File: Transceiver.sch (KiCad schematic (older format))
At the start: 37 parts

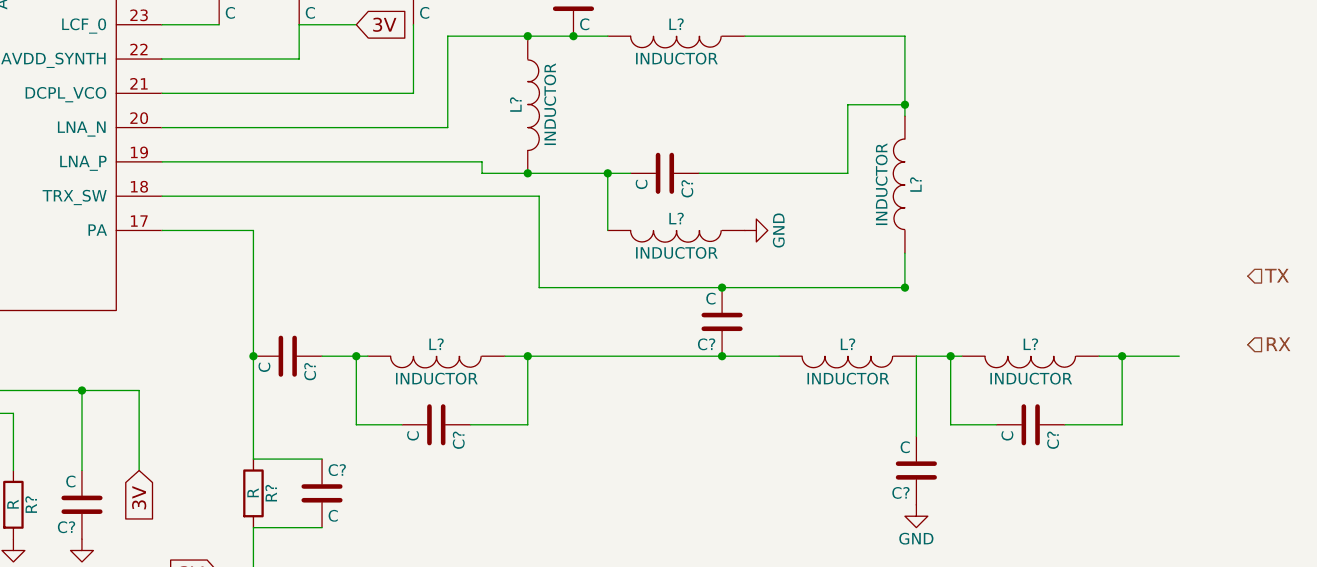
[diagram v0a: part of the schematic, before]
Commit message: took out the mcu schematic, fixed transciever for separate tx rx ports
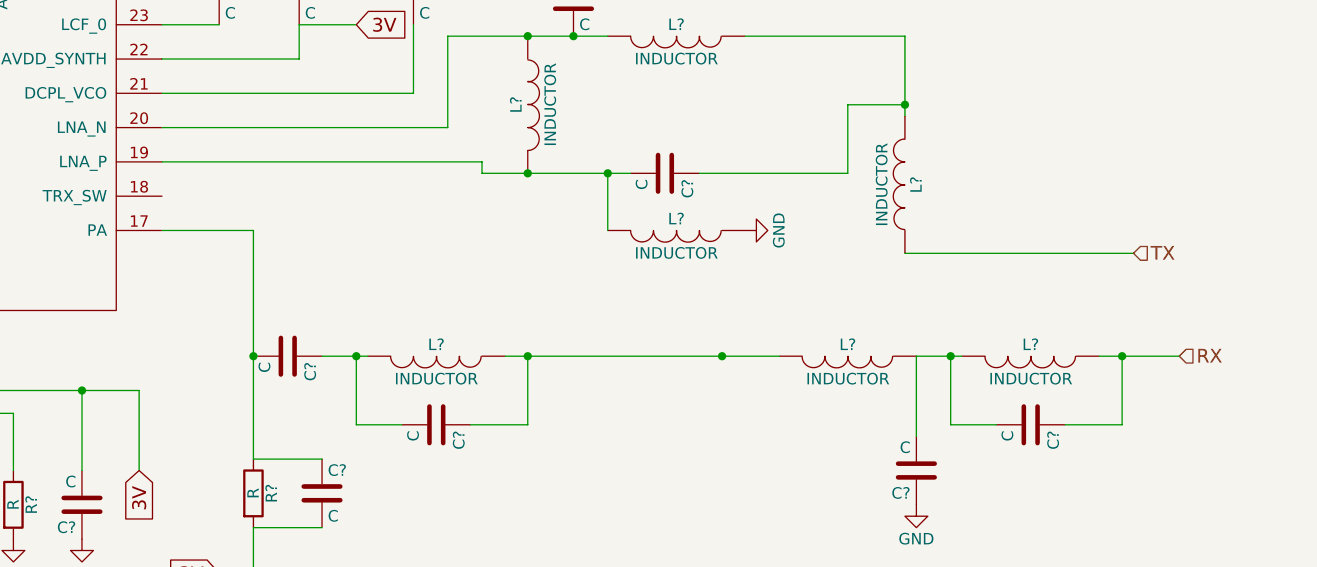
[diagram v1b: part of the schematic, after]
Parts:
- removed C?: C, symbol C
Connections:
- net RX: now also C?.1, L?.1
- net TX: now also L?.1
- net at U?.18 (TRX_SW): no longer L?.1
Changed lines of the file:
@@
-$Comp
-L C C?
-U 1 1 5821C907
-P 7800 4600
-F 0 "C?" H 7825 4700 50  0000 L CNN
-F 1 "C" H 7825 4500 50  0000 L CNN
-F 2 "" H 7838 4450 50  0000 C CNN
-F 3 "" H 7800 4600 50  0000 C CNN
-	1    7800 4600
-	-1   0    0    1
-$EndComp
 $Comp
 L C C?
@@
 Connection ~ 8600 3650
 Wire Wire Line
-	5350 4050 7000 4050
-Wire Wire Line
-	7000 4050 7000 4450
-Wire Wire Line
-	8600 4450 8600 4300
-Connection ~ 8600 4450
-Wire Wire Line
 	5350 4200 5750 4200
 Wire Wire Line
@@
 Wire Wire Line
 	6050 5700 6050 5900
-Wire Wire Line
-	7000 4450 8600 4450
-Connection ~ 7800 4450
 Wire Wire Line
 	4600 4750 4600 4800
@@
 Text HLabel 3850 4750 3    60   Input ~ 0
 CSN
-Text HLabel 10100 4700 2    60   Input ~ 0
+Text HLabel 9800 4750 2    60   Input ~ 0
 RX
-Text HLabel 10100 4400 2    60   Input ~ 0
+Text HLabel 9600 4300 2    60   Input ~ 0
 TX
+Wire Wire Line
+	9600 4300 8600 4300
 $EndSCHEMATC

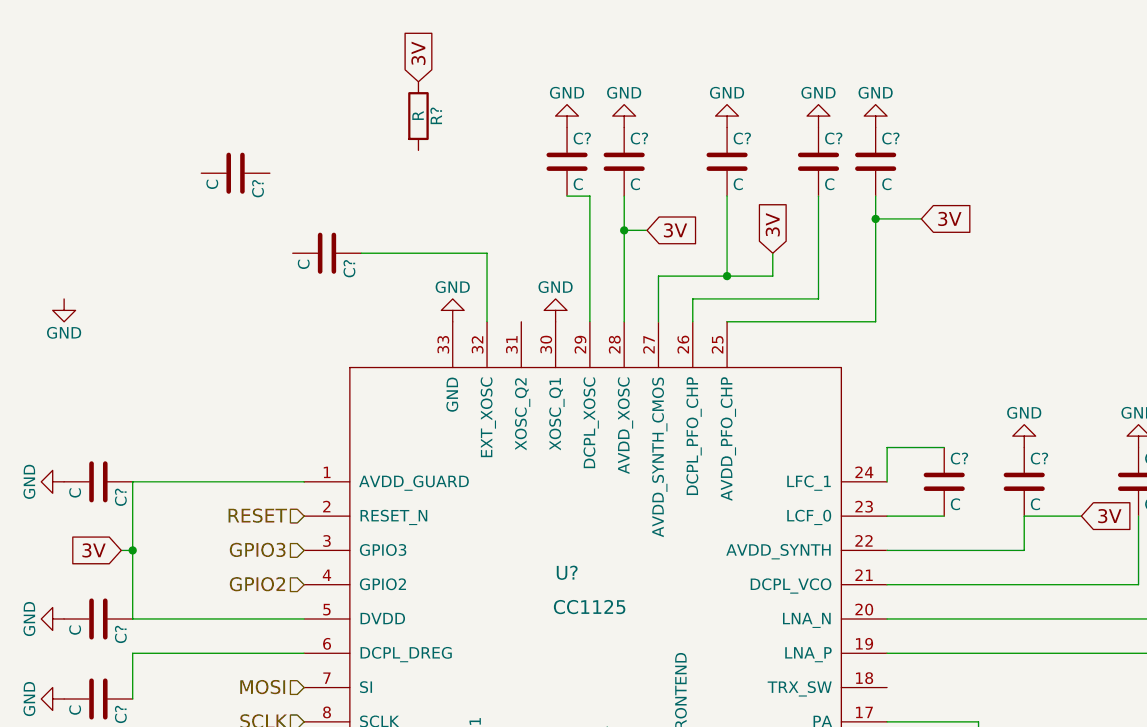
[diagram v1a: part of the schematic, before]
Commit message: deleted MCU schematic for v0.1. Added power sub-schematic
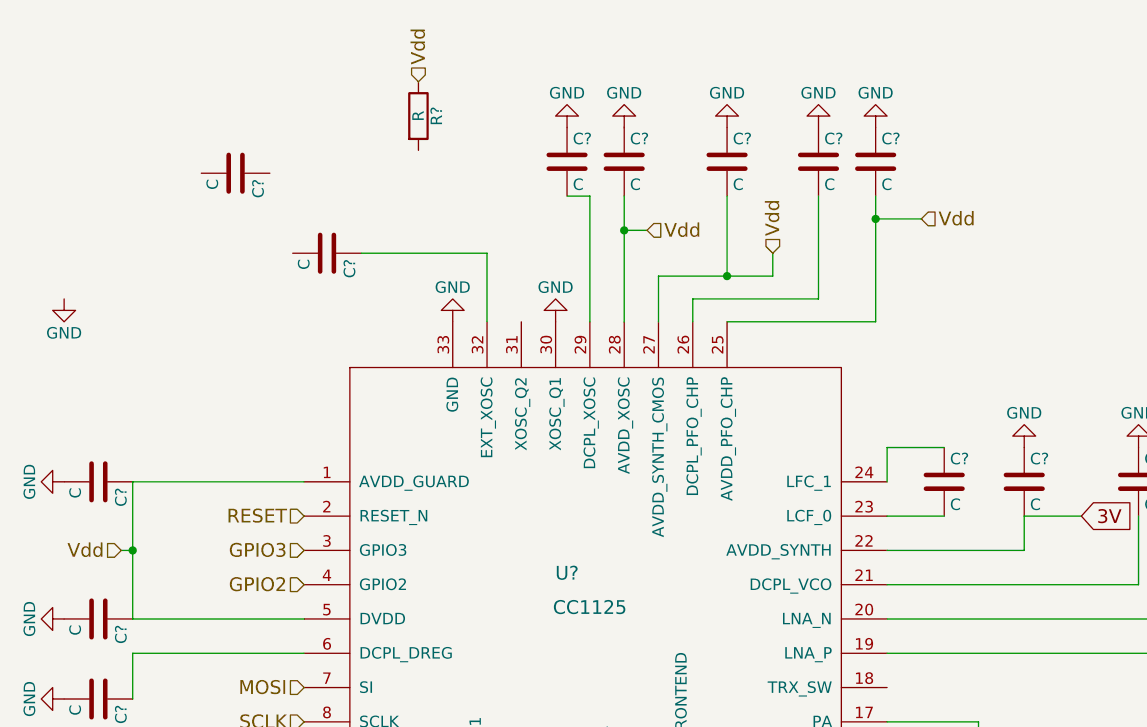
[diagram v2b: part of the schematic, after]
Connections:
- net 3V: no longer C?.1, C?.1, C?.2, C?.2, C?.2, R?.1, U?.1 (AVDD_GUARD), U?.25 (AVDD_PFO_CHP), U?.27 (AVDD_SYNTH_CMOS), U?.28 (AVDD_XOSC), U?.5 (DVDD)
- new net Vdd: C?.1, C?.1, C?.2, C?.2, C?.2, R?.1, U?.1 (AVDD_GUARD), U?.25 (AVDD_PFO_CHP), U?.27 (AVDD_SYNTH_CMOS), U?.28 (AVDD_XOSC), U?.5 (DVDD)
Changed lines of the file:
@@
 	-1   0    0    1
 $EndComp
-Text GLabel 2000 3450 0    60   Input ~ 0
-3V
 $Comp
 L C C?
@@
 	1    0    0    -1
 $EndComp
-Text GLabel 5500 2000 2    60   Input ~ 0
-3V
-Text GLabel 4850 2150 1    60   Input ~ 0
-3V
-Text GLabel 4300 2050 2    60   Input ~ 0
-3V
-Text GLabel 3300 1400 1    60   Input ~ 0
-3V
 Text HLabel 2800 3300 0    60   Input ~ 0
 RESET
@@
 Wire Wire Line
 	9600 4300 8600 4300
+Text HLabel 2000 3450 0    60   Input ~ 0
+Vdd
+Text HLabel 3300 1400 1    60   Input ~ 0
+Vdd
+Text HLabel 4300 2050 2    60   Input ~ 0
+Vdd
+Text HLabel 4850 2150 1    60   Input ~ 0
+Vdd
+Text HLabel 5500 2000 2    60   Input ~ 0
+Vdd
 $EndSCHEMATC

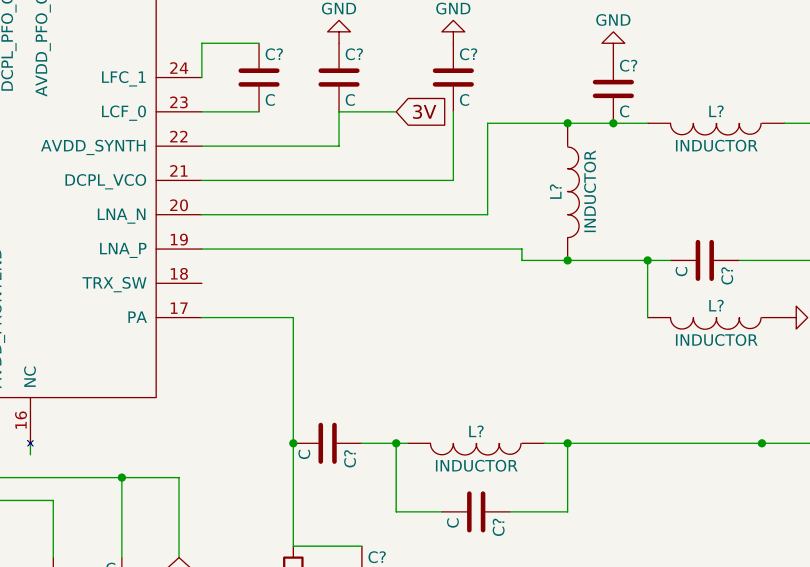
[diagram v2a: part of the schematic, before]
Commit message: added SKY65366-21 schematic and footprint to library. Populated front end schematic with SKY and peripherial components. Added 3V6 output for power sub-schematic.
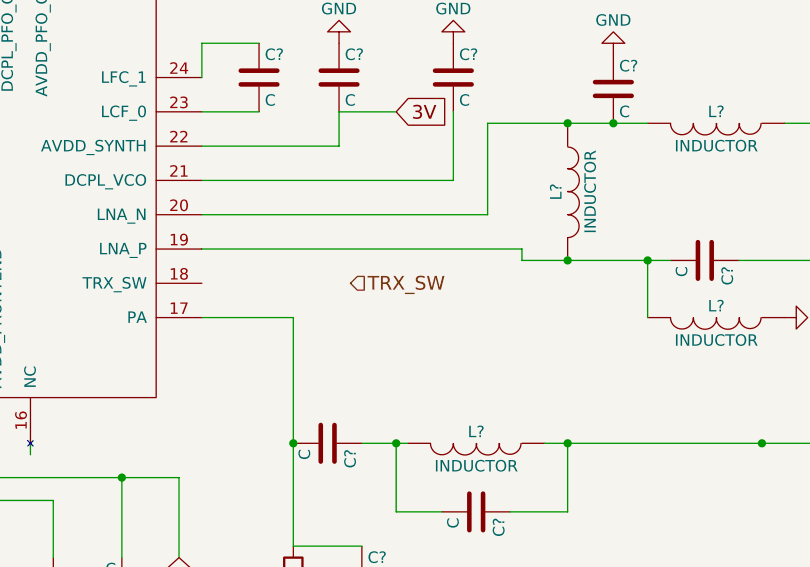
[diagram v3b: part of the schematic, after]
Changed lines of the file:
@@
 Text HLabel 5500 2000 2    60   Input ~ 0
 Vdd
+Text HLabel 6000 4050 2    60   Input ~ 0
+TRX_SW
 $EndSCHEMATC

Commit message: added BALF-112X-02D3 to component library and to transciever sub-schematic
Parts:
- removed C? (x9): C, symbol C
- removed L? (x7): INDUCTOR, symbol INDUCTOR
- removed R?: R, symbol R
- added C? (x2): C, symbol C
- added L?: INDUCTOR, symbol INDUCTOR
- added R?: R, symbol R
- added U?: BALF-112X-02D3, symbol BALF-112X-02D3
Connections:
- net labels added: 3V3, TRX_OPEN, TRX_SIG
- net labels removed: 3V, TRX_SW, Vdd
- wire segments 76 -> 60
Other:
- note added: "Add SPDT RF switch to component \nlibrary and schematic"
- note added: "TRX_OPEN is a active open drain when in TX mode, \nhigh impedence when in RX. TRX_SW requirs active \n3V3 high when in TX mode and GND when in RX \nmode (both low impedence)"
- note added: "add XOSC to component \nlibrary and to schematic\n"
- moved on the sheet: C?, R?, U?

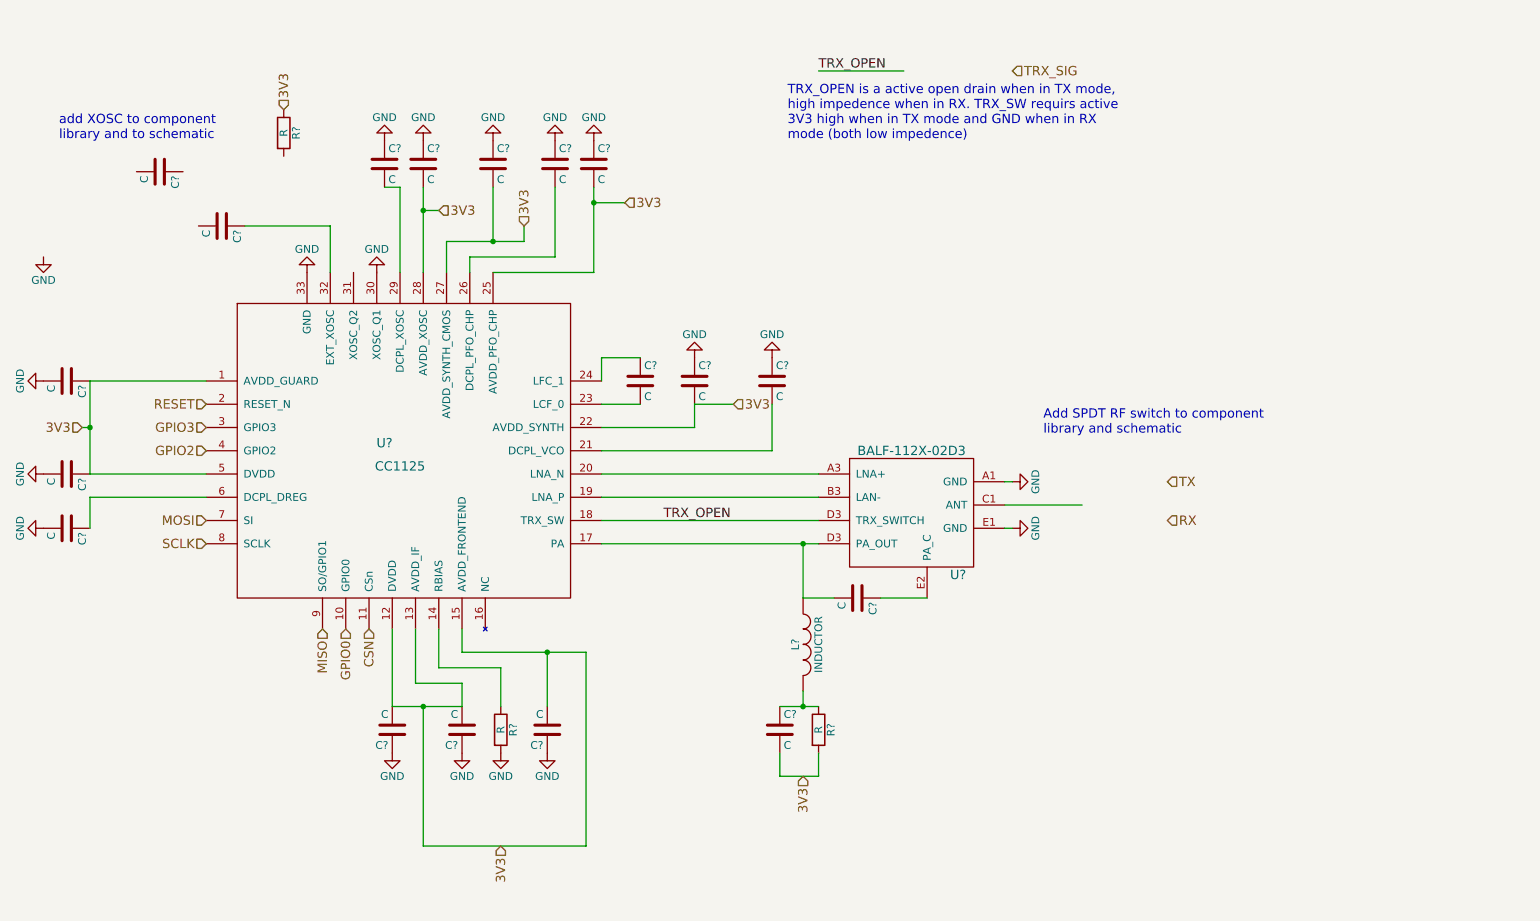
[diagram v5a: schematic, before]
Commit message: Added RF switch to transciever schematic
-Removed SMA lib pointing to Tobi's downloads
-Added SKY13372-467LF to the library (symbol and decal)
-Renamed signal “TX_SW” on RF front end page to “TRX_SIG”
-Re-aligned some part names and reference designators
-Added some component values to the front end
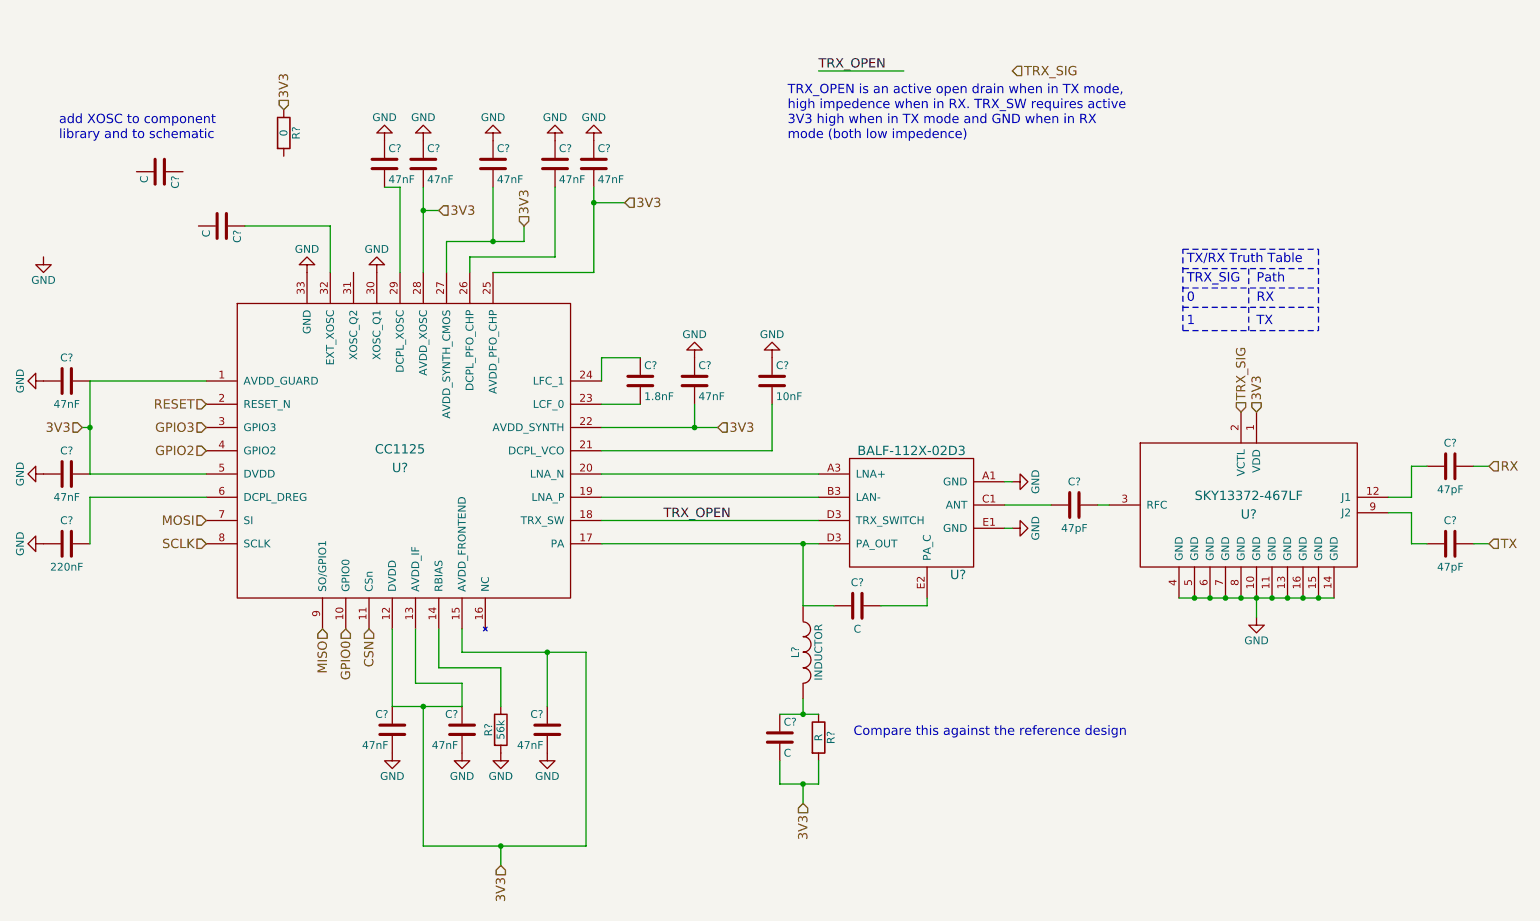
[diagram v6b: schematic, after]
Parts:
- added C? (x3): 47pF, symbol C
- added U?: SKY13372-467LF, symbol SKY13372-467LF
- C? (x11): value C -> 47nF
- C?: value C -> 220nF
- C?: value C -> 1.8nF
- C?: value C -> 10nF
- R?: value R -> 56k
- R?: value R -> 0
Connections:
- wire segments 60 -> 73
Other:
- note added: "0"
- note added: "1\n"
- note added: "Compare this against the reference design"
- note added: "Path"
- note added: "RX"
- note added: "TRX_OPEN is an active open drain when in TX mode, \nhigh impedence when in RX. TRX_SW requires active \n3V3 high when in TX mode and GND when in RX \nmode (both low impedence)"
- note added: "TRX_SIG"
- note added: "TX"
- note added: "TX/RX Truth Table"
- note removed: "Add SPDT RF switch to component \nlibrary and schematic"
- note removed: "TRX_OPEN is a active open drain when in TX mode, \nhigh impedence when in RX. TRX_SW requirs active \n3V3 high when in TX mode and GND when in RX \nmode (both low impedence)"
- moved on the sheet: C?, L?, R?
